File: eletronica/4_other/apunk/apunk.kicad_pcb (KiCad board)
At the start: 2 copper layers, 15 parts, among them J1 JACK_2P, SW1 SPST, U1 LM555N, U2 LM555N

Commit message: 
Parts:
- turned RV2 to 270 degrees
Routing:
- net +9V: track 133.1 -> 117.8 mm, vias 1 -> 2
- net N-0000013: track 19.9 -> 29.3 mm
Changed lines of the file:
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@@
   (general
     (links 31)
-    (no_connects 0)
+    (no_connects 1)
     (area 74.281667 59.445368 137.7044 117.665001)
     (thickness 1.6)
     (drawings 6)
-    (tracks 88)
+    (tracks 92)
     (zones 0)
     (modules 15)
@@
   )
   (module bornier3 (layer F.Cu)
-    (at 130.81 88.9 90)
+    (at 130.81 88.9 270)
     (descr "Bornier d'alimentation 3 pins")
     (tags DEV)
-    (fp_text reference RV2 (at 0 -5.08 90) (layer F.SilkS)
+    (fp_text reference RV2 (at 0 -5.08 270) (layer F.SilkS)
       (effects (font (size 1.524 1.524) (thickness 0.3048)))
     )
-    (fp_text value 500K (at 0 5.08 90) (layer F.SilkS)
+    (fp_text value 500K (at 0 5.08 270) (layer F.SilkS)
       (effects (font (size 1.524 1.524) (thickness 0.3048)))
     )
@@
     (fp_line (start -7.62 -3.81) (end 7.62 -3.81) (layer F.SilkS) (width 0.3048))
     (fp_line (start -7.62 3.81) (end 7.62 3.81) (layer F.SilkS) (width 0.3048))
-    (pad 1 thru_hole rect (at -5.08 0 90) (size 2.54 2.54) (drill 1.524)
+    (pad 1 thru_hole rect (at -5.08 0 270) (size 2.54 2.54) (drill 1.524)
       (layers *.Cu *.Mask F.SilkS)
       (net 1 +9V)
     )
-    (pad 2 thru_hole circle (at 0 0 90) (size 2.54 2.54) (drill 1.524)
+    (pad 2 thru_hole circle (at 0 0 270) (size 2.54 2.54) (drill 1.524)
       (layers *.Cu *.Mask F.SilkS)
       (net 1 +9V)
     )
-    (pad 3 thru_hole circle (at 5.08 0 90) (size 2.54 2.54) (drill 1.524)
+    (pad 3 thru_hole circle (at 5.08 0 270) (size 2.54 2.54) (drill 1.524)
       (layers *.Cu *.Mask F.SilkS)
       (net 7 N-0000013)
@@
     (arrow2b (pts (xy 78.74 63.5) (xy 79.32642 64.626503)))
   )
-  (segment (start 82.55 88.9) (end 87.63 88.9) (width 0.9) (layer F.Cu) (net 1) (status 400000))
-  (segment (start 106.68 85.09) (end 107.95 83.82) (width 0.9) (layer B.Cu) (net 1) (status 800000))
+  (segment (start 130.81 88.9) (end 129.54 88.9) (width 0.9) (layer F.Cu) (net 1) (status C00000))
+  (segment (start 116.84 104.14) (end 113.03 100.33) (width 0.9) (layer B.Cu) (net 1) (status 800000))
+  (segment (start 119.38 104.14) (end 116.84 104.14) (width 0.9) (layer B.Cu) (net 1))
+  (segment (start 120.65 105.41) (end 119.38 104.14) (width 0.9) (layer B.Cu) (net 1))
+  (via (at 120.65 105.41) (size 0.889) (layers F.Cu B.Cu) (net 1))
+  (segment (start 124.46 101.6) (end 120.65 105.41) (width 0.9) (layer F.Cu) (net 1))
+  (segment (start 124.46 93.98) (end 124.46 101.6) (width 0.9) (layer F.Cu) (net 1))
+  (segment (start 129.54 88.9) (end 124.46 93.98) (width 0.9) (layer F.Cu) (net 1) (status 400000))
+  (segment (start 82.55 88.9) (end 87.63 88.9) (width 0.9) (layer F.Cu) (net 1))
+  (segment (start 106.68 85.09) (end 107.95 83.82) (width 0.9) (layer B.Cu) (net 1))
   (segment (start 100.33 85.09) (end 106.68 85.09) (width 0.9) (layer B.Cu) (net 1))
   (via (at 100.33 85.09) (size 0.889) (layers F.Cu B.Cu) (net 1))
   (segment (start 91.44 85.09) (end 100.33 85.09) (width 0.9) (layer F.Cu) (net 1))
   (segment (start 87.63 88.9) (end 91.44 85.09) (width 0.9) (layer F.Cu) (net 1))
-  (segment (start 113.03 100.33) (end 125.73 113.03) (width 0.9) (layer B.Cu) (net 1))
-  (segment (start 130.81 111.76) (end 130.81 93.98) (width 0.9) (layer B.Cu) (net 1))
-  (segment (start 129.54 113.03) (end 130.81 111.76) (width 0.9) (layer B.Cu) (net 1))
-  (segment (start 128.27 113.03) (end 129.54 113.03) (width 0.9) (layer B.Cu) (net 1))
-  (segment (start 125.73 113.03) (end 128.27 113.03) (width 0.9) (layer B.Cu) (net 1))
   (segment (start 94.02064 111.71936) (end 95.29064 111.71936) (width 0.9) (layer B.Cu) (net 1))
   (segment (start 109.22 100.33) (end 113.03 100.33) (width 0.9) (layer B.Cu) (net 1))
@@
   (segment (start 83.82 113.03) (end 82.55 111.76) (width 0.9) (layer B.Cu) (net 1))
   (segment (start 82.55 93.98) (end 82.55 88.9) (width 0.9) (layer B.Cu) (net 1))
-  (segment (start 130.81 88.9) (end 130.81 93.98) (width 0.9) (layer B.Cu) (net 1))
   (segment (start 113.03 92.71) (end 115.57 92.71) (width 0.9) (layer F.Cu) (net 2))
   (segment (start 114.3 109.22) (end 113.03 109.22) (width 0.9) (layer F.Cu) (net 2))
@@
   (segment (start 128.27 100.33) (end 123.19 95.25) (width 0.9) (layer B.Cu) (net 6))
   (segment (start 123.19 95.25) (end 120.65 95.25) (width 0.9) (layer B.Cu) (net 6))
+  (segment (start 130.81 93.98) (end 127 93.98) (width 0.9) (layer B.Cu) (net 7))
+  (segment (start 124.46 82.55) (end 120.65 78.74) (width 0.9) (layer B.Cu) (net 7))
+  (segment (start 124.46 91.44) (end 124.46 82.55) (width 0.9) (layer B.Cu) (net 7))
+  (segment (start 127 93.98) (end 124.46 91.44) (width 0.9) (layer B.Cu) (net 7))
   (segment (start 115.57 78.74) (end 115.57 81.28) (width 0.9) (layer B.Cu) (net 7))
   (segment (start 120.65 78.74) (end 115.57 78.74) (width 0.9) (layer B.Cu) (net 7))
-  (segment (start 130.81 83.82) (end 125.73 83.82) (width 0.9) (layer B.Cu) (net 7))
-  (segment (start 125.73 83.82) (end 120.65 78.74) (width 0.9) (layer B.Cu) (net 7))
   (segment (start 101.6 73.66) (end 101.6 78.74) (width 0.9) (layer B.Cu) (net 8))
   (segment (start 113.03 95.25) (end 114.3 95.25) (width 0.9) (layer B.Cu) (net 9))

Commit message: 
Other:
- board text added: "ATARI PUNK CONSOLE"
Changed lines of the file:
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@@
-(kicad_pcb (version 3) (host pcbnew "(2013-may-18)-stable")
+(kicad_pcb (version 3) (host pcbnew "(2013-05-16 BZR 4016)-stable")
   (general
     (links 31)
@@
     (area 74.281667 59.445368 137.7044 117.665001)
     (thickness 1.6)
-    (drawings 6)
+    (drawings 7)
     (tracks 92)
     (zones 0)
@@
     (pad_to_mask_clearance 0)
     (aux_axis_origin 0 0)
-    (visible_elements FFFFFFBF)
+    (visible_elements 7FFFFFFF)
     (pcbplotparams
-      (layerselection 3178497)
-      (usegerberextensions true)
+      (layerselection 32769)
+      (usegerberextensions false)
       (excludeedgelayer true)
       (linewidth 0.150000)
@@
       (padsonsilk false)
       (subtractmaskfromsilk false)
-      (outputformat 1)
+      (outputformat 2)
       (mirror false)
-      (drillshape 1)
+      (drillshape 0)
       (scaleselection 1)
       (outputdirectory ""))
@@
     )
   )
+  (gr_text "ATARI\nPUNK\nCONSOLE" (at 93.98 91.44) (layer F.Cu)
+    (effects (font (size 2 2) (thickness 0.3)))
+  )
   (gr_line (start 132.08 114.3) (end 132.08 63.5) (angle 90) (layer Eco1.User) (width 0.2))
   (gr_line (start 81.28 114.3) (end 132.08 114.3) (angle 90) (layer Eco1.User) (width 0.2))
@@
     (arrow2b (pts (xy 78.74 63.5) (xy 79.32642 64.626503)))
   )
-  (segment (start 130.81 88.9) (end 129.54 88.9) (width 0.9) (layer F.Cu) (net 1) (status C00000))
-  (segment (start 116.84 104.14) (end 113.03 100.33) (width 0.9) (layer B.Cu) (net 1) (status 800000))
+  (segment (start 130.81 88.9) (end 129.54 88.9) (width 0.9) (layer F.Cu) (net 1))
+  (segment (start 116.84 104.14) (end 113.03 100.33) (width 0.9) (layer B.Cu) (net 1))
   (segment (start 119.38 104.14) (end 116.84 104.14) (width 0.9) (layer B.Cu) (net 1))
   (segment (start 120.65 105.41) (end 119.38 104.14) (width 0.9) (layer B.Cu) (net 1))
@@
   (segment (start 124.46 101.6) (end 120.65 105.41) (width 0.9) (layer F.Cu) (net 1))
   (segment (start 124.46 93.98) (end 124.46 101.6) (width 0.9) (layer F.Cu) (net 1))
-  (segment (start 129.54 88.9) (end 124.46 93.98) (width 0.9) (layer F.Cu) (net 1) (status 400000))
+  (segment (start 129.54 88.9) (end 124.46 93.98) (width 0.9) (layer F.Cu) (net 1))
   (segment (start 82.55 88.9) (end 87.63 88.9) (width 0.9) (layer F.Cu) (net 1))
   (segment (start 106.68 85.09) (end 107.95 83.82) (width 0.9) (layer B.Cu) (net 1))

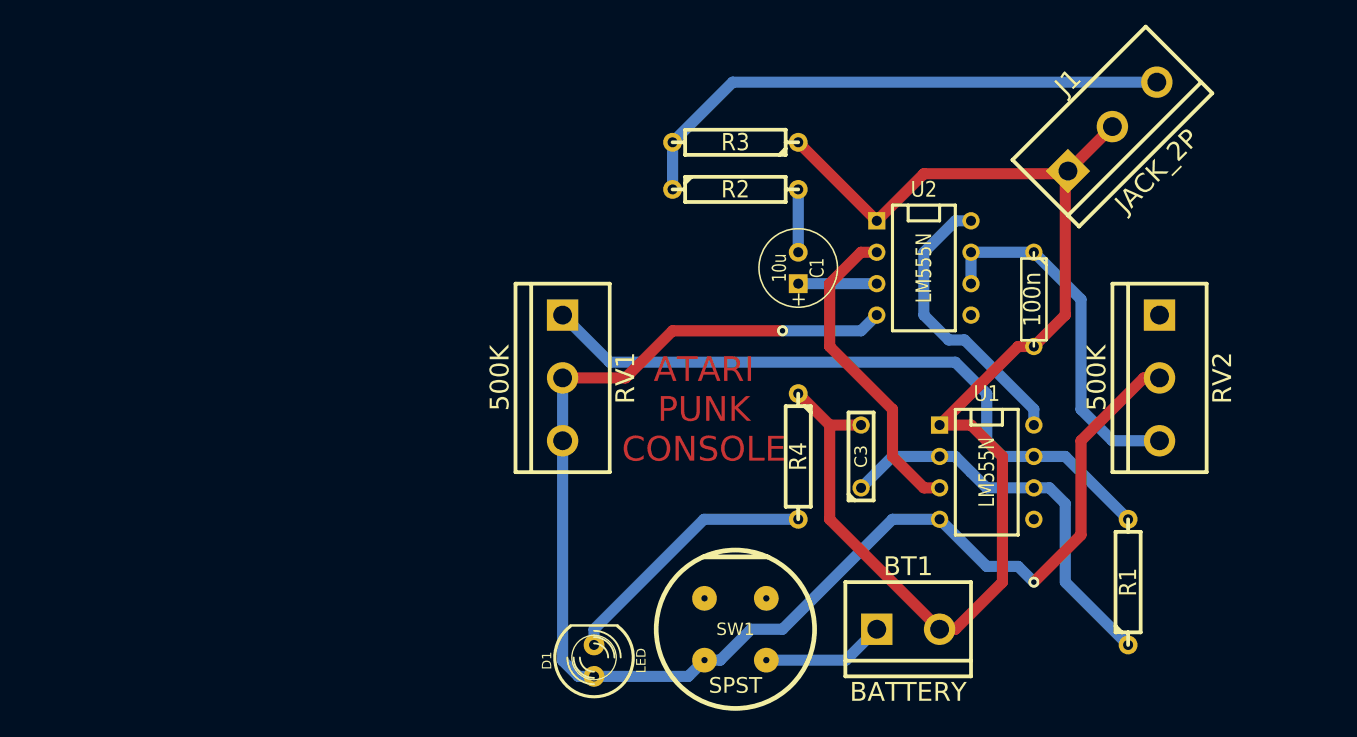
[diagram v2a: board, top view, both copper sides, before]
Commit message: 
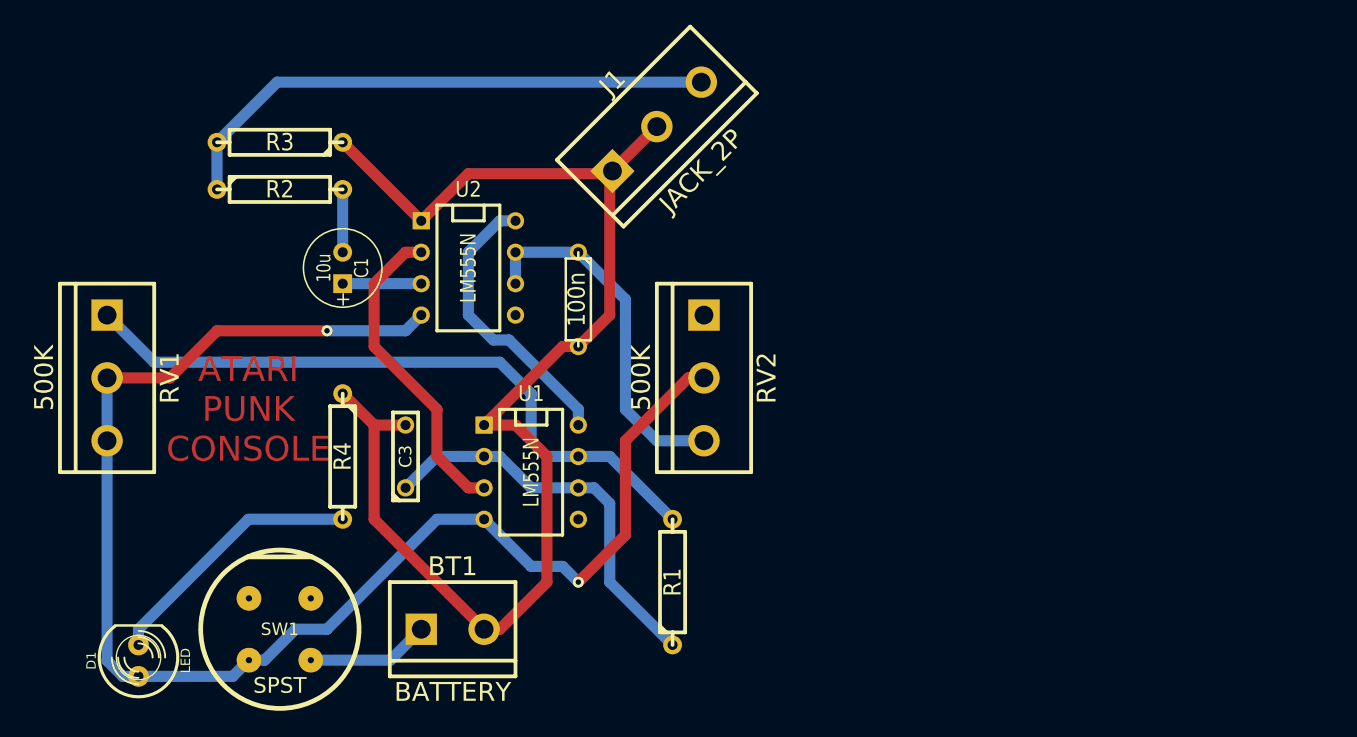
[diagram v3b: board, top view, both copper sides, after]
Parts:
- moved C3 36.8 mm to (69.8, 95.2)
- moved C4 36.8 mm to (83.8, 82.5)
- moved R1 36.8 mm to (91.4, 105.4)
- moved D1 36.8 mm to (48.3, 111.8)
- moved BT1 36.8 mm to (73.7, 109.2)
- moved C1 36.8 mm to (64.8, 80.0)
- moved J1 36.8 mm to (90.2, 68.6)
- moved R2 36.8 mm to (59.7, 73.7)
- moved R3 36.8 mm to (59.7, 69.8)
- moved R4 36.8 mm to (64.8, 95.2)
- moved RV1 36.8 mm to (45.7, 88.9)
- moved RV2 36.8 mm to (94.0, 88.9)
- moved SW1 36.8 mm to (59.7, 109.2)
- moved U1 36.8 mm to (80.0, 96.5)
- moved U2 36.8 mm to (74.9, 80.0)

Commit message: 
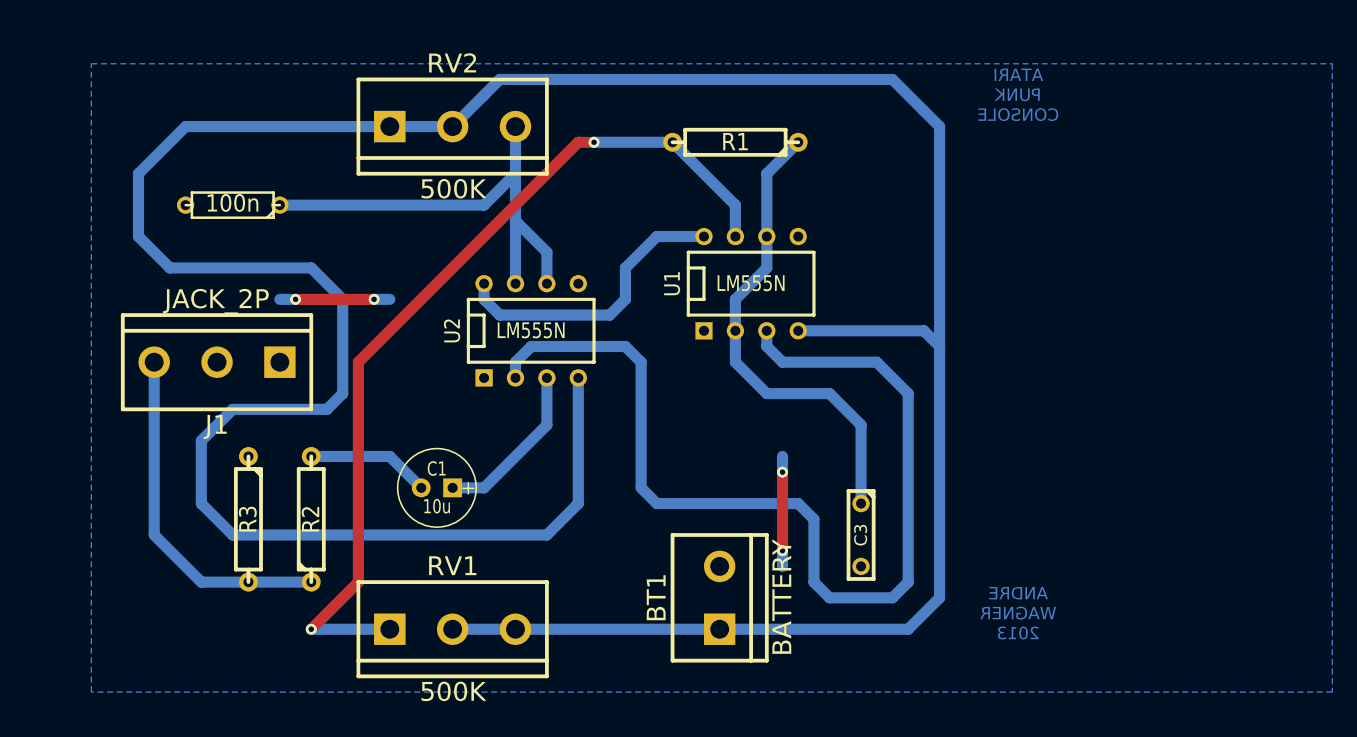
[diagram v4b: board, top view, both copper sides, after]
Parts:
- removed D1: LED, LED-5MM
- removed R4: 680, R4
- removed SW1: SPST, PUSH_BUTT_SHAPE1
- moved J1 40.3 mm to (54.6, 87.6), turned to 180 degrees
- moved C3 37.4 mm to (106.7, 101.6), turned to 270 degrees
- moved R1 35.9 mm to (96.5, 69.8), turned to 180 degrees
- moved RV1 34.5 mm to (73.7, 109.2), turned to 0 degrees
- moved R3 30.6 mm to (57.1, 100.3), turned to 270 degrees
- moved C4 29.0 mm to (55.9, 74.9), turned to 180 degrees
- moved RV2 28.7 mm to (73.7, 68.6), turned to 0 degrees
- moved R2 26.8 mm to (62.2, 100.3), turned to 90 degrees
- moved U1 23.4 mm to (97.8, 81.3), turned to 0 degrees
- moved BT1 21.7 mm to (95.2, 106.7), turned to 90 degrees
- moved C1 19.3 mm to (72.4, 97.8), turned to 180 degrees
- moved U2 7.18 mm to (80.0, 85.1), turned to 0 degrees
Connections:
- BT1 pad 1: N-000001 -> +9V
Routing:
- net +9V: track 117.8 -> 252.1 mm, vias 2 -> 0
- net GND: track 106.0 -> 17.8 mm, vias 0 -> 4
- net N-000006: track 25.8 -> 80.9 mm
- net N-000008: track 21.5 -> 0.00 mm
- net N-000007: track 54.8 -> 72.0 mm, vias 0 -> 2
- net N-000003: track 45.0 -> 28.2 mm
- net N-000001: track 9.97 -> 0.00 mm
- net N-0000010: track 29.3 -> 38.9 mm
- net N-0000011: track 6.35 -> 13.5 mm
- net N-000009: track 32.7 -> 38.5 mm
- net N-0000012: track 5.08 -> 9.94 mm
- added copper zone on B.Cu, net GND
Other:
- board text added: "ANDRE WAGNER 2013"
